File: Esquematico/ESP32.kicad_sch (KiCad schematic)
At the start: 9 parts, among them U3 ESP32-WROOM-32

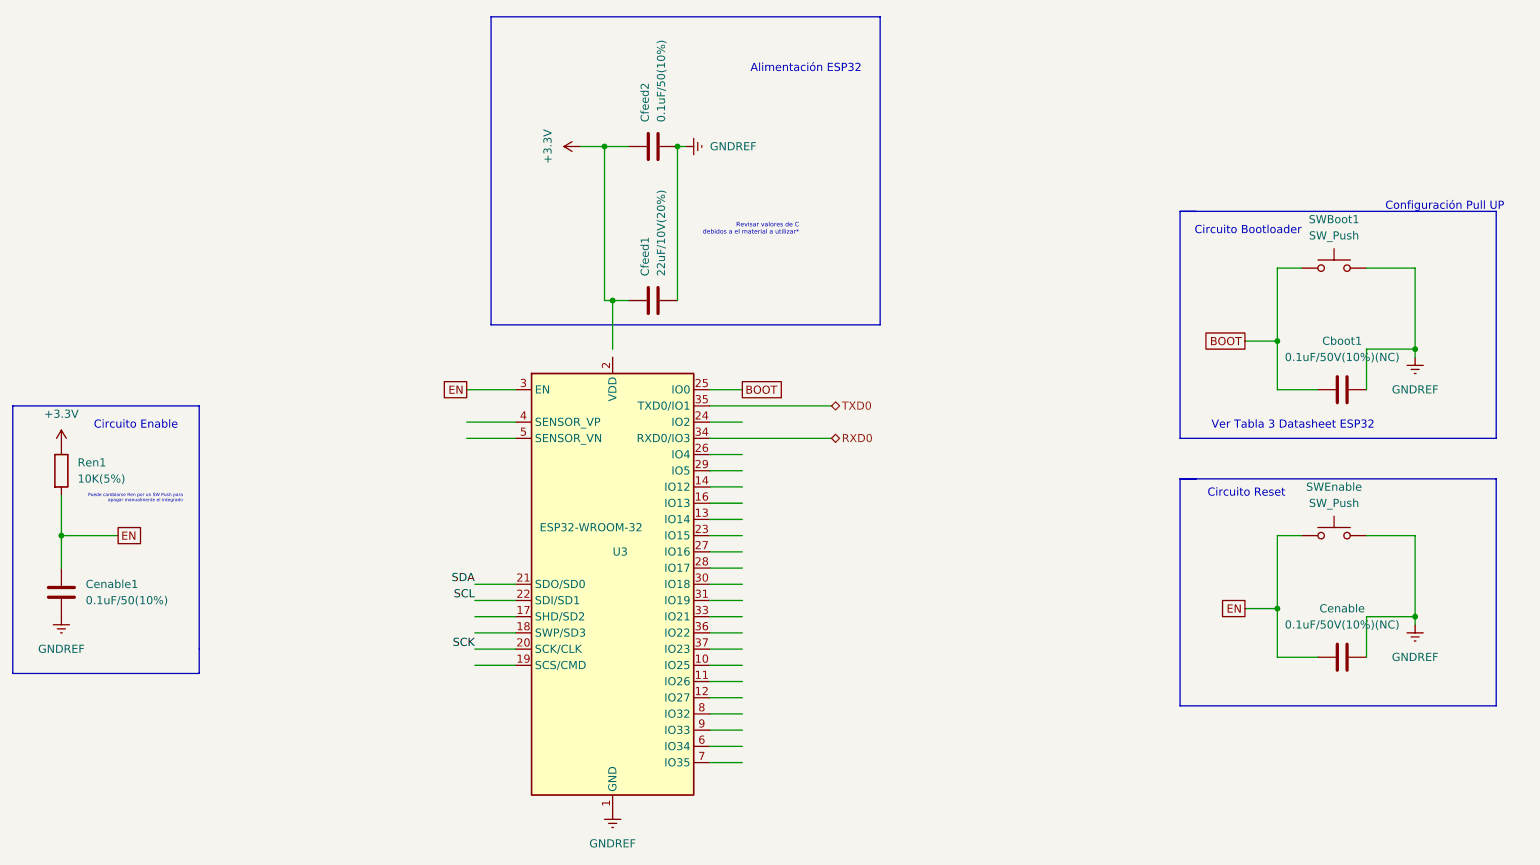
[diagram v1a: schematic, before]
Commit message: Circuito Pantalla Oled SSD1306 implementado. Modelo y Footprints SD1306 agregados
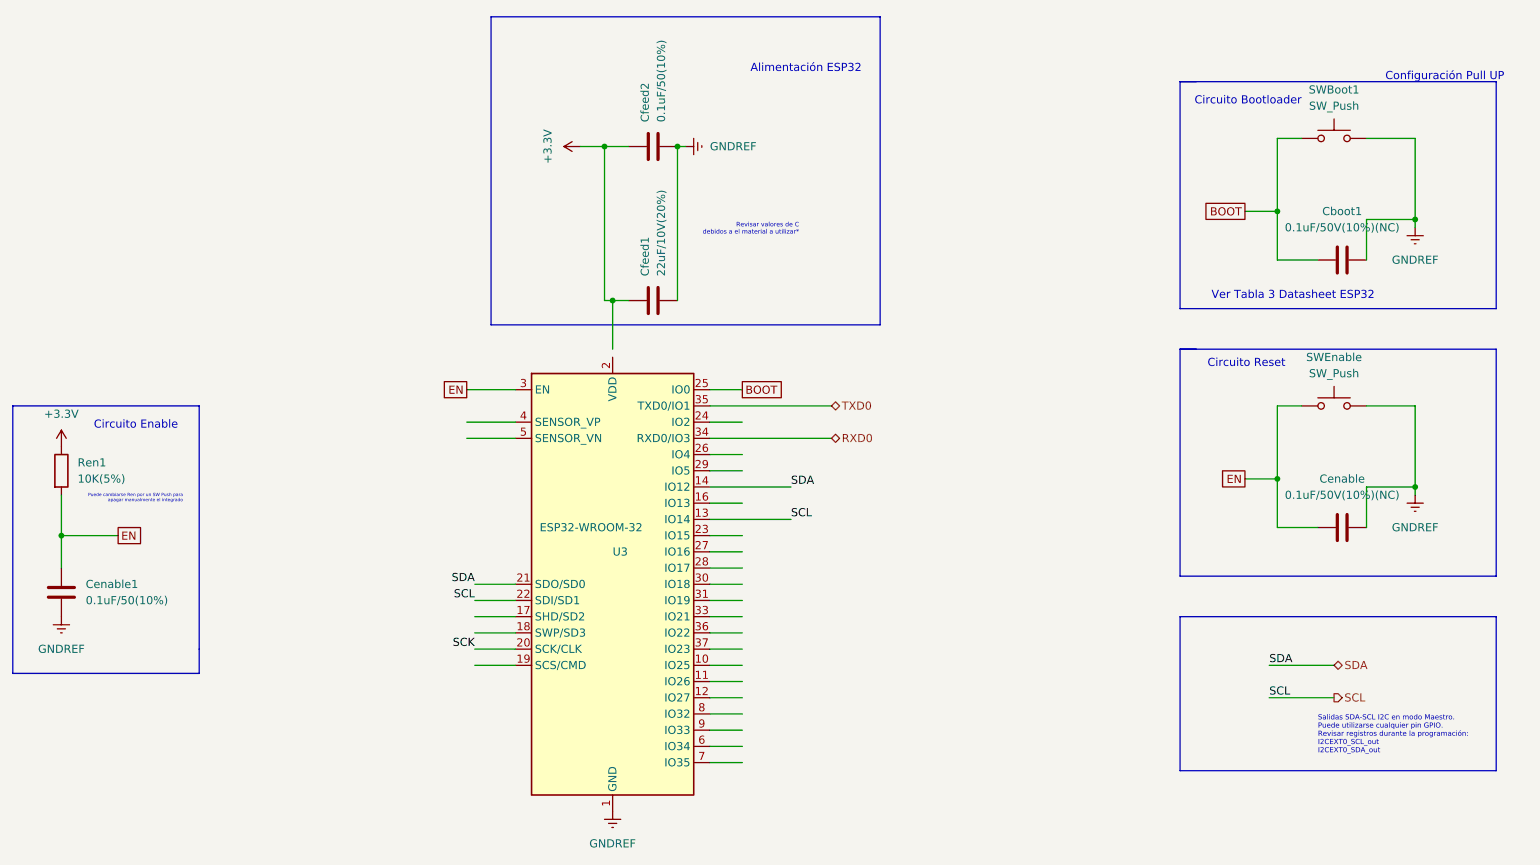
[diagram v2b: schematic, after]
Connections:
- net SCL: now also U3.13 (IO14)
- net SDA: now also U3.14 (IO12)
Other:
- note added: "Salidas SDA-SCL I2C en modo Maestro. Puede utilizarse cualquier pin GPIO. Revisar registros durante la programación: I2CEXT0_SCL_out I2CEXT0_SDA_out"
- moved on the sheet: Cboot1, Cenable, SWBoot1, SWEnable

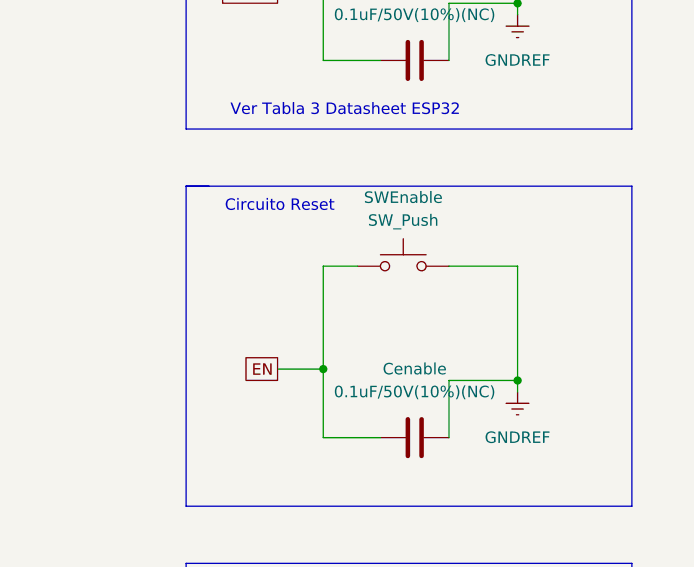
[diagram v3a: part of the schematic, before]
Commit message: actualizacion huellas resitencias y capacitorees
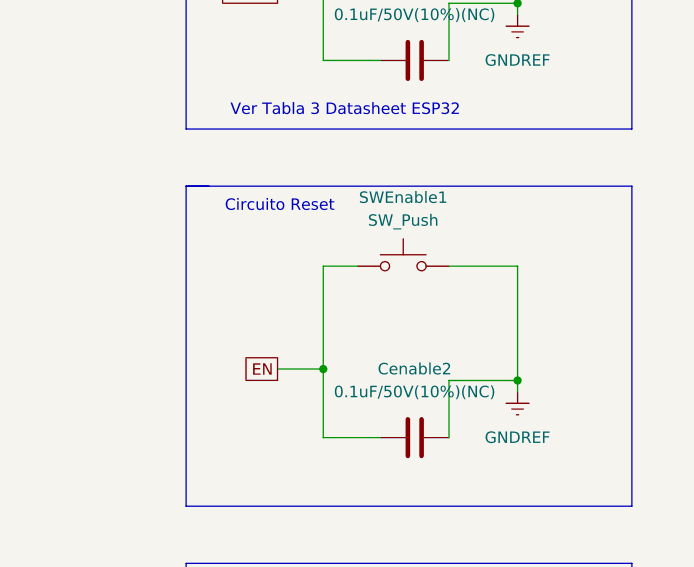
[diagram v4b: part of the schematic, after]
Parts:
- Cboot1, Cfeed1: footprint (none) -> Capacitor_SMD:C_0805_2012Metric_Pad1.18x1.45mm_HandSolder
- Cenable1, Cfeed2: footprint Capacitor_SMD:C_1210_3225Metric_Pad1.33x2.70mm_HandSolder -> Capacitor_SMD:C_0805_2012Metric_Pad1.18x1.45mm_HandSolder
- Cenable2: renamed from Cenable; footprint (none) -> Capacitor_SMD:C_0805_2012Metric_Pad1.18x1.45mm_HandSolder
- Ren1: footprint (none) -> Resistor_SMD:R_0805_2012Metric_Pad1.20x1.40mm_HandSolder
- SWBoot1: footprint (none) -> Button_Switch_SMD:SW_Push_1P1T_NO_6x6mm_H9.5mm
- SWEnable1: renamed from SWEnable; footprint (none) -> Button_Switch_SMD:SW_Push_1P1T_NO_6x6mm_H9.5mm
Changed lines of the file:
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@@
   )
   (text "Puede cambiarse Ren por un SW Push para \napagar manualmente el integrado"
-    (at 63.5 101.6 0)
+    (at 63.5 101.6 180)
     (effects (font (size 0.5 0.5)) (justify right bottom))
   )
@@
   )
   (text "Revisar valores de C \ndebidos a el material a utilizar*\n"
-    (at 160.02 59.69 0)
+    (at 160.02 59.69 180)
     (effects (font (size 0.7 0.7)) (justify right bottom))
   )
@@
   (symbol (lib_id "power:GNDREF") (at 256.54 100.33 0) (unit 1)
     (in_bom yes) (on_board yes) (fields_autoplaced)
-    (property "Reference" "#PWR?" (id 0) (at 256.54 106.68 0)
+    (property "Reference" "#PWR0129" (id 0) (at 256.54 106.68 0)
       (effects (font (size 1.27 1.27)) hide)
     )
@@
     (property "Reference" "SWBoot1" (id 0) (at 243.84 36.83 0))
     (property "Value" "SW_Push" (id 1) (at 243.84 39.37 0))
-    (property "Footprint" "" (id 2) (at 243.84 39.37 0)
+    (property "Footprint" "Button_Switch_SMD:SW_Push_1P1T_NO_6x6mm_H9.5mm" (id 2) (at 243.84 39.37 0)
       (effects (font (size 1.27 1.27)) hide)
     )
@@
   (symbol (lib_id "Device:C") (at 245.11 105.41 90) (unit 1)
     (in_bom yes) (on_board yes) (fields_autoplaced)
-    (property "Reference" "Cenable" (id 0) (at 245.11 97.79 90))
+    (property "Reference" "Cenable2" (id 0) (at 245.11 97.79 90))
     (property "Value" "0.1uF/50V(10%)(NC)" (id 1) (at 245.11 100.33 90))
-    (property "Footprint" "" (id 2) (at 248.92 104.4448 0)
+    (property "Footprint" "Capacitor_SMD:C_0805_2012Metric_Pad1.18x1.45mm_HandSolder" (id 2) (at 248.92 104.4448 0)
       (effects (font (size 1.27 1.27)) hide)
     )
@@
       (effects (font (size 1.27 1.27)) (justify left))
     )
-    (property "Footprint" "" (id 2) (at 42.672 96.52 90)
+    (property "Footprint" "Resistor_SMD:R_0805_2012Metric_Pad1.20x1.40mm_HandSolder" (id 2) (at 42.672 96.52 90)
       (effects (font (size 1.27 1.27)) hide)
     )
@@
       (effects (font (size 1.27 1.27)) (justify right))
     )
-    (property "Footprint" "Capacitor_SMD:C_1210_3225Metric_Pad1.33x2.70mm_HandSolder" (id 2) (at 133.35 46.6852 0)
+    (property "Footprint" "Capacitor_SMD:C_0805_2012Metric_Pad1.18x1.45mm_HandSolder" (id 2) (at 133.35 46.6852 0)
       (effects (font (size 1.27 1.27)) hide)
     )
@@
   (symbol (lib_id "Switch:SW_Push") (at 243.84 86.36 0) (unit 1)
     (in_bom yes) (on_board yes) (fields_autoplaced)
-    (property "Reference" "SWEnable" (id 0) (at 243.84 78.74 0))
+    (property "Reference" "SWEnable1" (id 0) (at 243.84 78.74 0))
     (property "Value" "SW_Push" (id 1) (at 243.84 81.28 0))
-    (property "Footprint" "" (id 2) (at 243.84 81.28 0)
+    (property "Footprint" "Button_Switch_SMD:SW_Push_1P1T_NO_6x6mm_H9.5mm" (id 2) (at 243.84 81.28 0)
       (effects (font (size 1.27 1.27)) hide)
     )
@@
       (effects (font (size 1.27 1.27)) (justify left))
     )
-    (property "Footprint" "" (id 2) (at 140.97 68.8848 0)
+    (property "Footprint" "Capacitor_SMD:C_0805_2012Metric_Pad1.18x1.45mm_HandSolder" (id 2) (at 140.97 68.8848 0)
       (effects (font (size 1.27 1.27)) hide)
     )
@@
     (property "Reference" "Cboot1" (id 0) (at 245.11 55.88 90))
     (property "Value" "0.1uF/50V(10%)(NC)" (id 1) (at 245.11 58.42 90))
-    (property "Footprint" "" (id 2) (at 248.92 62.5348 0)
+    (property "Footprint" "Capacitor_SMD:C_0805_2012Metric_Pad1.18x1.45mm_HandSolder" (id 2) (at 248.92 62.5348 0)
       (effects (font (size 1.27 1.27)) hide)
     )
@@
       (effects (font (size 1.27 1.27)) (justify right))
     )
-    (property "Footprint" "Capacitor_SMD:C_1210_3225Metric_Pad1.33x2.70mm_HandSolder" (id 2) (at 43.4848 111.76 0)
-      (effects (font (size 1.27 1.27)) hide)
-    )
+    (property "Footprint" "Capacitor_SMD:C_0805_2012Metric_Pad1.18x1.45mm_HandSolder" (id 2) (at 43.4848 111.76 0)
+      (effects (font (size 1.27 1.27)) hide)
+    )
